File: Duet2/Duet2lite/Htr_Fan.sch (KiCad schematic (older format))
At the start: 32 parts, among them J3 5V V_FAN VIN, U11 74HCT02

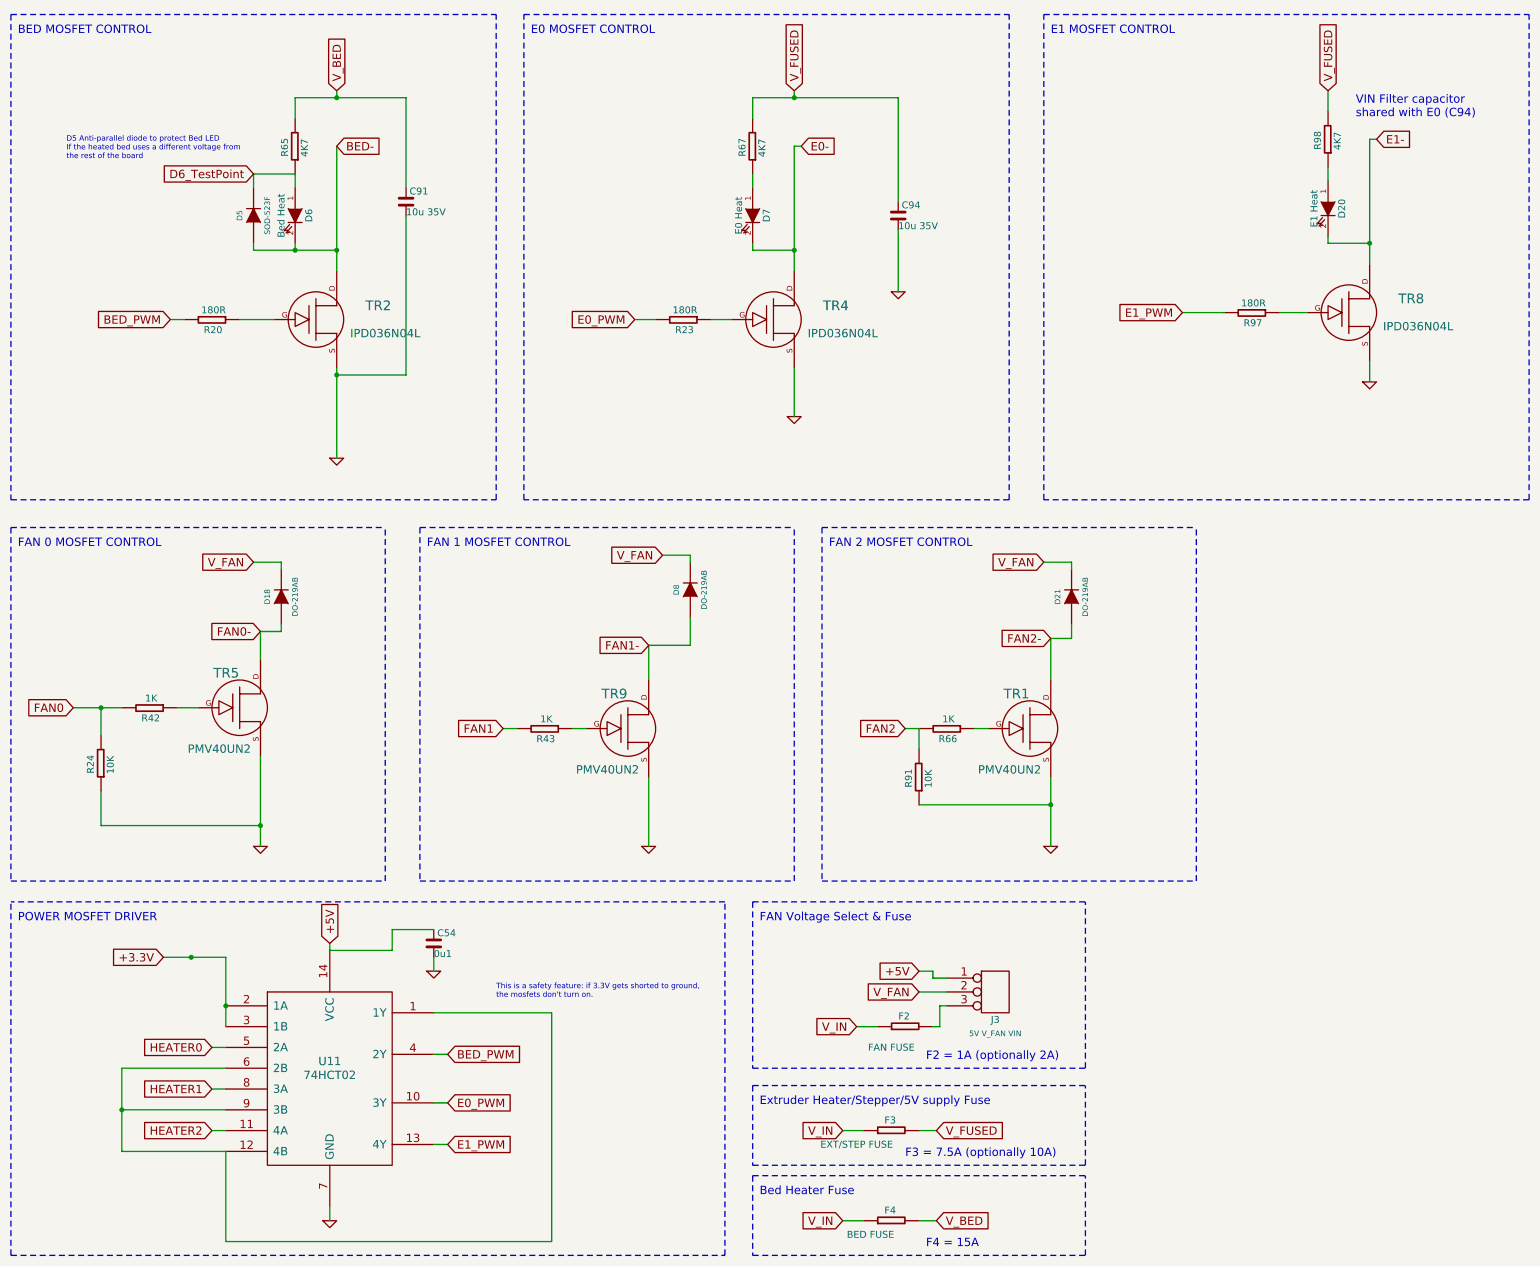
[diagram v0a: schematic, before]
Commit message: removed stepper drivers from the schematic
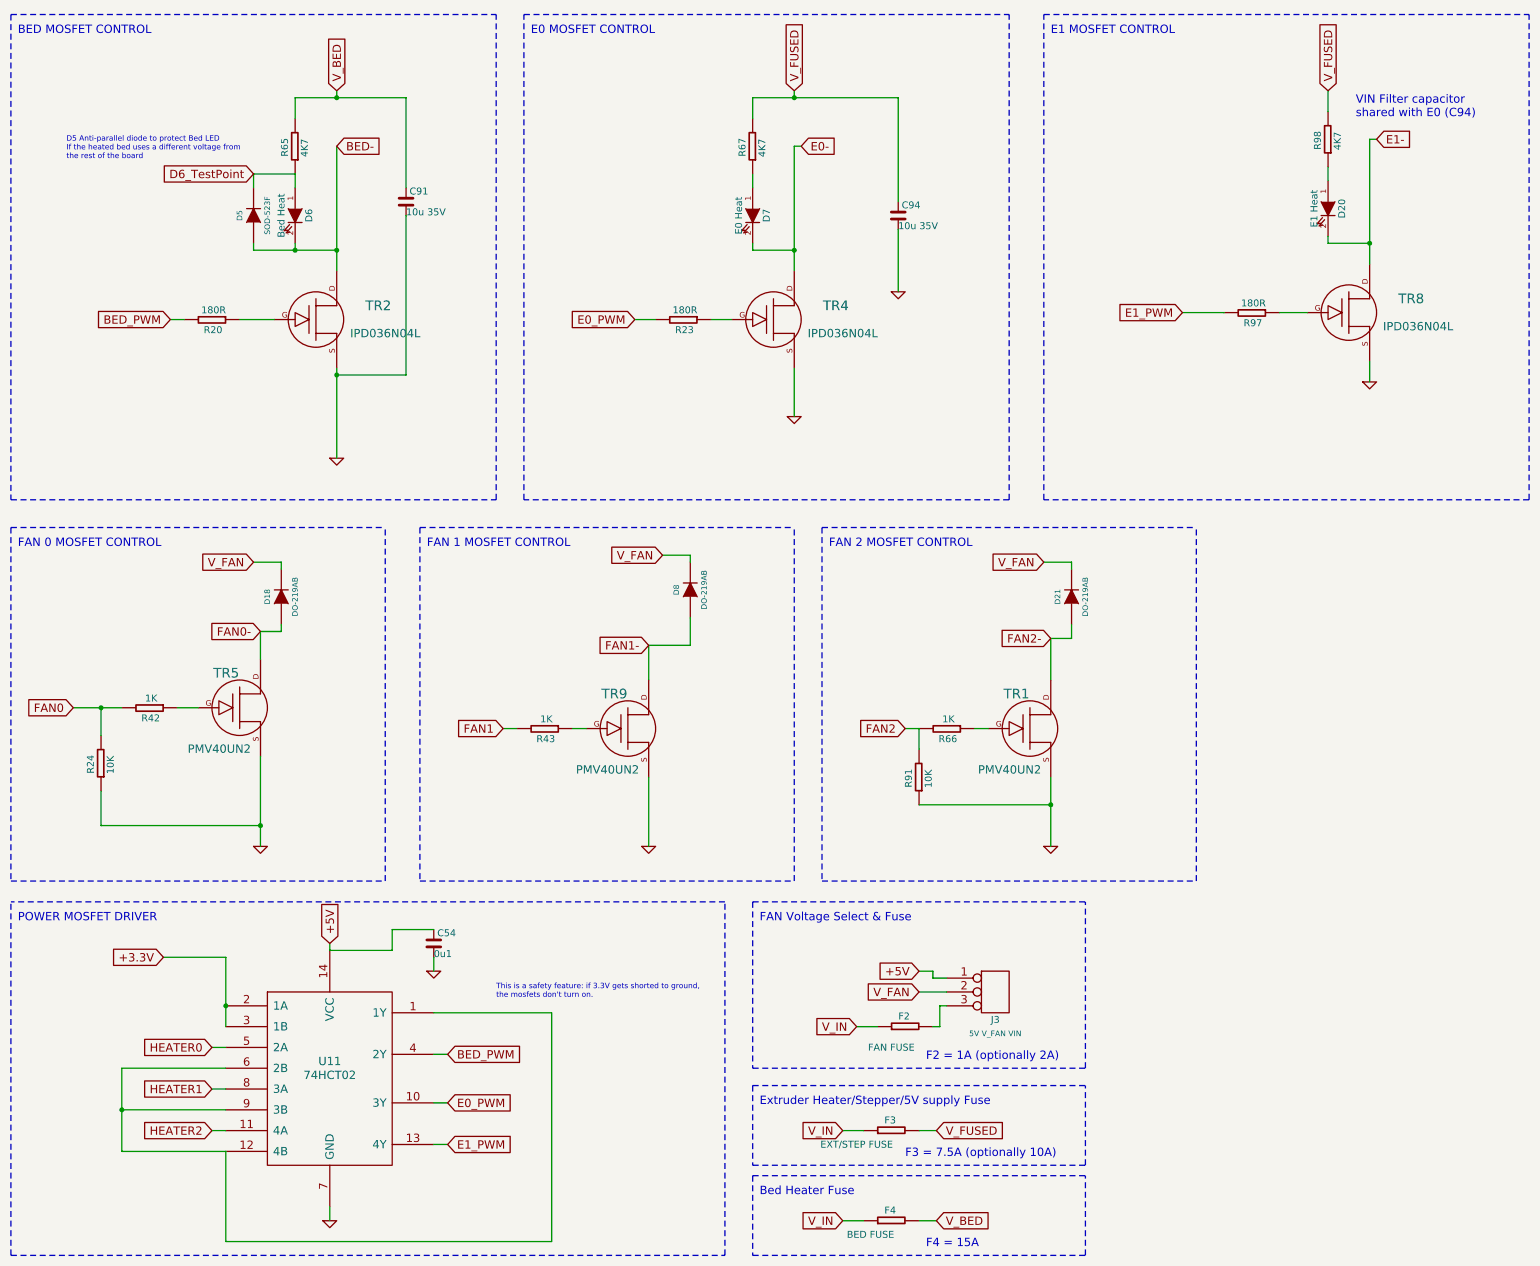
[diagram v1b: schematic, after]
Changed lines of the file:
@@
 Connection ~ 6600 1850
 Wire Wire Line
-	6300 1850 7350 1850
+	6300 1850 6600 1850
 Wire Wire Line
 	7350 1850 7350 2600
@@
 Connection ~ 3300 1850
 Wire Wire Line
-	3000 1850 3800 1850
+	3000 1850 3300 1850
 Wire Wire Line
 	3800 1850 3800 2500
 Wire Wire Line
-	1400 6250 1750 6250
+	1400 6250 1600 6250
 Wire Wire Line
 	2100 3450 2200 3450
@@
 	6650 2200 6600 2200
 Wire Wire Line
-	6600 2200 6600 3100
-Wire Wire Line
-	3300 3800 3300 4450
-Wire Wire Line
-	3300 2200 3300 3100
+	6600 2200 6600 2950
+Wire Wire Line
+	3300 3800 3300 3850
+Wire Wire Line
+	3300 2200 3300 2950
 Wire Notes Line
 	950  4950 3650 4950
@@
 	3000 2900 3000 2950
 Wire Wire Line
-	2700 2950 3300 2950
+	2700 2950 3000 2950
 Connection ~ 3300 2950
 Wire Wire Line
-	2750 6600 2750 7250
+	2750 6600 2750 7100
 Wire Wire Line
 	6300 2400 6300 2500
@@
 P 2750 7250
 AR Path="/5090541F" Ref="#PWR053"  Part="1"
-AR Path="/50577A22/5090541F" Ref="#PWR77"  Part="1"
-F 0 "#PWR77" H 2750 7250 30  0001 C CNN
+AR Path="/50577A22/5090541F" Ref="#PWR077"  Part="1"
+F 0 "#PWR077" H 2750 7250 30  0001 C CNN
 F 1 "GND" H 2750 7180 30  0001 C CNN
 F 2 "" H 2750 7250 60  0001 C CNN
@@
 P 6600 4150
 AR Path="/50905416" Ref="#PWR054"  Part="1"
-AR Path="/50577A22/50905416" Ref="#PWR82"  Part="1"
-F 0 "#PWR82" H 6600 4150 30  0001 C CNN
+AR Path="/50577A22/50905416" Ref="#PWR082"  Part="1"
+F 0 "#PWR082" H 6600 4150 30  0001 C CNN
 F 1 "GND" H 6600 4080 30  0001 C CNN
 F 2 "" H 6600 4150 60  0001 C CNN
@@
 P 3300 4450
 AR Path="/5064BB75" Ref="#PWR055"  Part="1"
-AR Path="/50577A22/5064BB75" Ref="#PWR79"  Part="1"
-F 0 "#PWR79" H 3300 4450 30  0001 C CNN
+AR Path="/50577A22/5064BB75" Ref="#PWR079"  Part="1"
+F 0 "#PWR079" H 3300 4450 30  0001 C CNN
 F 1 "GND" H 3300 4380 30  0001 C CNN
 F 2 "" H 3300 4450 60  0001 C CNN
@@
 	10800 2150 10750 2150
 Wire Wire Line
-	10750 2150 10750 3050
+	10750 2150 10750 2900
 Wire Notes Line
 	11900 4750 11900 1250
@@
 P 5550 7250
 AR Path="/5547E89A" Ref="#PWR057"  Part="1"
-AR Path="/50577A22/5547E89A" Ref="#PWR81"  Part="1"
-F 0 "#PWR81" H 5550 7250 30  0001 C CNN
+AR Path="/50577A22/5547E89A" Ref="#PWR081"  Part="1"
+F 0 "#PWR081" H 5550 7250 30  0001 C CNN
 F 1 "GND" H 5550 7180 30  0001 C CNN
 F 2 "" H 5550 7250 60  0001 C CNN
@@
 P 3250 9950
 AR Path="/568188CF" Ref="#PWR058"  Part="1"
-AR Path="/50577A22/568188CF" Ref="#PWR78"  Part="1"
-F 0 "#PWR78" H 3250 9950 30  0001 C CNN
+AR Path="/50577A22/568188CF" Ref="#PWR078"  Part="1"
+F 0 "#PWR078" H 3250 9950 30  0001 C CNN
 F 1 "GND" H 3250 9880 30  0001 C CNN
 F 2 "" H 3250 9950 60  0001 C CNN
@@
 $EndComp
 Wire Wire Line
-	2500 8050 2500 8550
+	2500 8050 2500 8400
 Wire Wire Line
 	4000 8450 4850 8450
@@
 	2500 9450 1750 9450
 Wire Wire Line
-	1750 9450 1750 8850
+	1750 9450 1750 9150
 Wire Wire Line
 	1750 9150 2500 9150
@@
 P 4000 8150
 AR Path="/56943D05" Ref="#PWR059"  Part="1"
-AR Path="/50577A22/56943D05" Ref="#PWR80"  Part="1"
-F 0 "#PWR80" H 4000 8150 30  0001 C CNN
+AR Path="/50577A22/56943D05" Ref="#PWR080"  Part="1"
+F 0 "#PWR080" H 4000 8150 30  0001 C CNN
 F 1 "GND" H 4000 8080 30  0001 C CNN
 F 2 "" H 4000 8150 60  0001 C CNN
@@
 	1    0    0    -1
 $EndComp
-Wire Wire Line
-	2050 8050 2500 8050
 Connection ~ 2500 8400
-Connection ~ 2250 8050
 Wire Wire Line
 	3250 8000 3700 8000
@@
 P 7350 3250
 AR Path="/56F6B8E3" Ref="#PWR060"  Part="1"
-AR Path="/50577A22/56F6B8E3" Ref="#PWR83"  Part="1"
-F 0 "#PWR83" H 7350 3250 30  0001 C CNN
+AR Path="/50577A22/56F6B8E3" Ref="#PWR083"  Part="1"
+F 0 "#PWR083" H 7350 3250 30  0001 C CNN
 F 1 "GND" H 7350 3180 30  0001 C CNN
 F 2 "" H 7350 3250 60  0001 C CNN
@@
 P 10750 3900
 AR Path="/56F6BC87" Ref="#PWR061"  Part="1"
-AR Path="/50577A22/56F6BC87" Ref="#PWR85"  Part="1"
-F 0 "#PWR85" H 10750 3900 30  0001 C CNN
+AR Path="/50577A22/56F6BC87" Ref="#PWR085"  Part="1"
+F 0 "#PWR085" H 10750 3900 30  0001 C CNN
 F 1 "GND" H 10750 3830 30  0001 C CNN
 F 2 "" H 10750 3900 60  0001 C CNN
@@
 	8450 5750 8450 6050
 Wire Wire Line
-	8450 6750 8450 7250
+	8450 6750 8450 6950
 $Comp
 L DuetWifi:BSH105 TR1
@@
 P 8450 7250
 AR Path="/571B8014" Ref="#PWR062"  Part="1"
-AR Path="/50577A22/571B8014" Ref="#PWR84"  Part="1"
-F 0 "#PWR84" H 8450 7250 30  0001 C CNN
+AR Path="/50577A22/571B8014" Ref="#PWR084"  Part="1"
+F 0 "#PWR084" H 8450 7250 30  0001 C CNN
 F 1 "GND" H 8450 7180 30  0001 C CNN
 F 2 "" H 8450 7250 60  0001 C CNN
@@
 Text Notes 7550 10150 0    60   ~ 0
 F4 = 15A
+Wire Wire Line
+	6600 1850 7350 1850
+Wire Wire Line
+	3300 1850 3800 1850
+Wire Wire Line
+	6600 2950 6600 3100
+Wire Wire Line
+	3300 2950 3300 3100
+Wire Wire Line
+	2750 7100 2750 7250
+Wire Wire Line
+	10750 2900 10750 3050
+Wire Wire Line
+	1600 6250 1750 6250
+Wire Wire Line
+	1750 9150 1750 8850
+Wire Wire Line
+	2500 8400 2500 8550
+Wire Wire Line
+	8450 6950 8450 7250
+Wire Wire Line
+	3000 2950 3300 2950
+Wire Wire Line
+	3300 3850 3300 4450
+Wire Wire Line
+	2050 8050 2500 8050
 $EndSCHEMATC
